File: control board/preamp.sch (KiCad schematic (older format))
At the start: 51 parts, among them U201 TL972, U202 MCP42100_VOL, U203 MCP42100_TREB, U204 MCP42100_BASS, U205 TL972

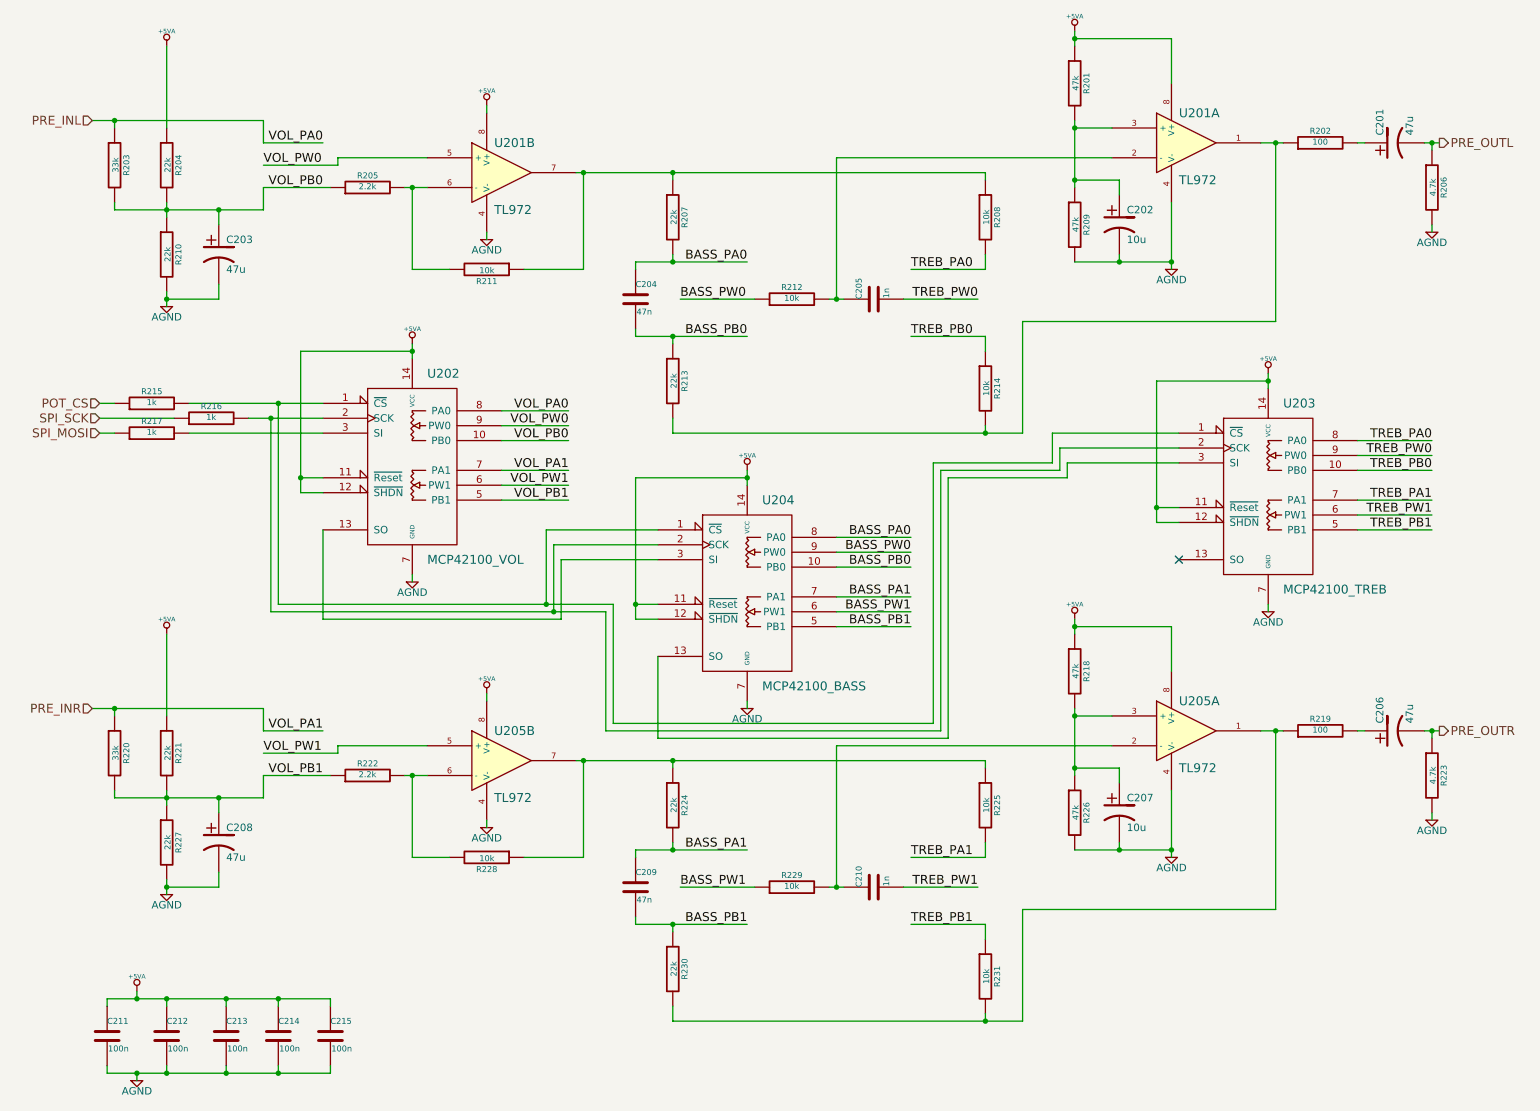
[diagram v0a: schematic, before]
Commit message: Fix capacitor polarity & prep for SMT
The control board and preamp are being prepared for SMT, and the CP1
module does not associate polarity correctly.
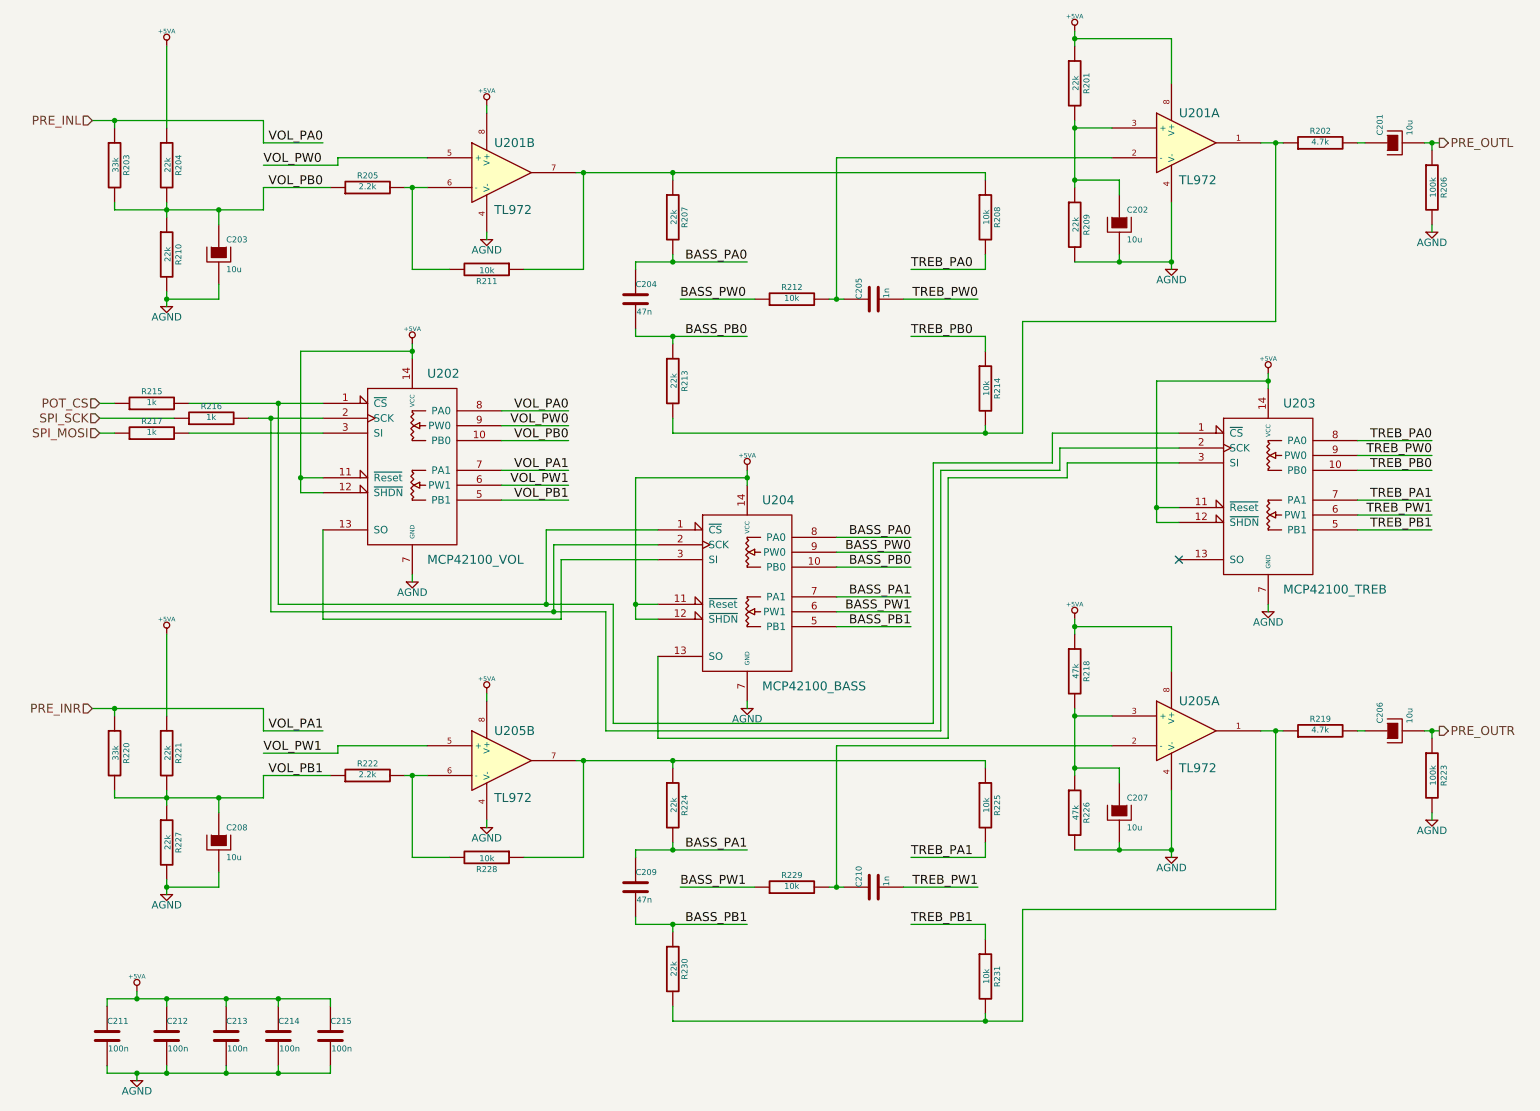
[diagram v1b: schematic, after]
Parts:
- removed C201, C203, C206, C208: 47u, ~, symbol CP1
- removed C202, C207: 10u, ~, symbol CP1
- added C201, C202, C203, C206, C207, C208: 10u, ~, symbol CAPAPOL
- R201, R209: value 47k -> 22k
- R202, R219: value 100 -> 4.7k
- R206, R223: value 4.7k -> 100k
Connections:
- net AGND: now also C202.2, C203.2, C207.2, C208.2
- net PRE_OUTL: now also C201.2
- net PRE_OUTR: now also C206.2
- net VOL_PB0: now also C203.1
- net VOL_PB1: now also C208.1
- net at R201.2, R209.1, U201.3 (+): now also C202.1
- net at R202.2: now also C201.1
- net at R218.2, R226.1, U205.3 (+): now also C207.1
- net at R219.2: now also C206.1
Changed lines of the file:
@@
 Sheet 2 2
 Title "AIA Rev. B Control Board Preamp"
-Date "8 mar 2014"
+Date "11 apr 2014"
 Rev "B01"
 Comp "Ali Kocaturk"
@@
 F 3 "~" H 1450 2100 30  0000 C CNN
 	1    1450 2100
-	1    0    0    -1
-$EndComp
-$Comp
-L CP1 C203
-U 1 1 531AED4E
-P 1800 2100
-F 0 "C203" H 1850 2200 50  0000 L CNN
-F 1 "47u" H 1850 2000 50  0000 L CNN
-F 2 "~" H 1800 2100 60  0000 C CNN
-F 3 "~" H 1800 2100 60  0000 C CNN
-	1    1800 2100
 	1    0    0    -1
 $EndComp
@@
 P 7550 950
 F 0 "R201" V 7630 950 40  0000 C CNN
-F 1 "47k" V 7557 951 40  0000 C CNN
+F 1 "22k" V 7557 951 40  0000 C CNN
 F 2 "~" V 7480 950 30  0000 C CNN
 F 3 "~" H 7550 950 30  0000 C CNN
@@
 P 7550 1900
 F 0 "R209" V 7630 1900 40  0000 C CNN
-F 1 "47k" V 7557 1901 40  0000 C CNN
+F 1 "22k" V 7557 1901 40  0000 C CNN
 F 2 "~" V 7480 1900 30  0000 C CNN
 F 3 "~" H 7550 1900 30  0000 C CNN
 	1    7550 1900
-	1    0    0    -1
-$EndComp
-$Comp
-L CP1 C202
-U 1 1 531A9735
-P 7850 1900
-F 0 "C202" H 7900 2000 50  0000 L CNN
-F 1 "10u" H 7900 1800 50  0000 L CNN
-F 2 "~" H 7850 1900 60  0000 C CNN
-F 3 "~" H 7850 1900 60  0000 C CNN
-	1    7850 1900
 	1    0    0    -1
 $EndComp
@@
 P 9200 1350
 F 0 "R202" V 9280 1350 40  0000 C CNN
-F 1 "100" V 9207 1351 40  0000 C CNN
+F 1 "4.7k" V 9207 1351 40  0000 C CNN
 F 2 "~" V 9130 1350 30  0000 C CNN
 F 3 "~" H 9200 1350 30  0000 C CNN
@@
 $EndComp
 $Comp
-L CP1 C201
-U 1 1 531A9D72
-P 9700 1350
-F 0 "C201" H 9750 1450 50  0000 L CNN
-F 1 "47u" H 9750 1250 50  0000 L CNN
-F 2 "~" H 9700 1350 60  0000 C CNN
-F 3 "~" H 9700 1350 60  0000 C CNN
-	1    9700 1350
-	0    -1   -1   0
-$EndComp
-$Comp
 L R R206
 U 1 1 531A9D81
 P 9950 1650
 F 0 "R206" V 10030 1650 40  0000 C CNN
-F 1 "4.7k" V 9957 1651 40  0000 C CNN
+F 1 "100k" V 9957 1651 40  0000 C CNN
 F 2 "~" V 9880 1650 30  0000 C CNN
 F 3 "~" H 9950 1650 30  0000 C CNN
@@
 F 3 "~" H 1450 6050 30  0000 C CNN
 	1    1450 6050
-	1    0    0    -1
-$EndComp
-$Comp
-L CP1 C208
-U 1 1 531AA135
-P 1800 6050
-F 0 "C208" H 1850 6150 50  0000 L CNN
-F 1 "47u" H 1850 5950 50  0000 L CNN
-F 2 "~" H 1800 6050 60  0000 C CNN
-F 3 "~" H 1800 6050 60  0000 C CNN
-	1    1800 6050
 	1    0    0    -1
 $EndComp
@@
 	1    0    0    -1
 $EndComp
-$Comp
-L CP1 C207
-U 1 1 531AA1DD
-P 7850 5850
-F 0 "C207" H 7900 5950 50  0000 L CNN
-F 1 "10u" H 7900 5750 50  0000 L CNN
-F 2 "~" H 7850 5850 60  0000 C CNN
-F 3 "~" H 7850 5850 60  0000 C CNN
-	1    7850 5850
-	1    0    0    -1
-$EndComp
 Connection ~ 7550 5200
 Wire Wire Line
@@
 P 9200 5300
 F 0 "R219" V 9280 5300 40  0000 C CNN
-F 1 "100" V 9207 5301 40  0000 C CNN
+F 1 "4.7k" V 9207 5301 40  0000 C CNN
 F 2 "~" V 9130 5300 30  0000 C CNN
 F 3 "~" H 9200 5300 30  0000 C CNN
@@
 $EndComp
 $Comp
-L CP1 C206
-U 1 1 531AA205
-P 9700 5300
-F 0 "C206" H 9750 5400 50  0000 L CNN
-F 1 "47u" H 9750 5200 50  0000 L CNN
-F 2 "~" H 9700 5300 60  0000 C CNN
-F 3 "~" H 9700 5300 60  0000 C CNN
-	1    9700 5300
-	0    -1   -1   0
-$EndComp
-$Comp
 L R R223
 U 1 1 531AA20B
 P 9950 5600
 F 0 "R223" V 10030 5600 40  0000 C CNN
-F 1 "4.7k" V 9957 5601 40  0000 C CNN
+F 1 "100k" V 9957 5601 40  0000 C CNN
 F 2 "~" V 9880 5600 30  0000 C CNN
 F 3 "~" H 9950 5600 30  0000 C CNN
@@
 	2550 7600 2550 7550
 Connection ~ 2200 7600
+$Comp
+L CAPAPOL C203
+U 1 1 53488C60
+P 1800 2100
+F 0 "C203" H 1850 2200 40  0000 L CNN
+F 1 "10u" H 1850 2000 40  0000 L CNN
+F 2 "~" H 1900 1950 30  0000 C CNN
+F 3 "~" H 1800 2100 300 0000 C CNN
+	1    1800 2100
+	1    0    0    -1
+$EndComp
+$Comp
+L CAPAPOL C202
+U 1 1 53488C7C
+P 7850 1900
+F 0 "C202" H 7900 2000 40  0000 L CNN
+F 1 "10u" H 7900 1800 40  0000 L CNN
+F 2 "~" H 7950 1750 30  0000 C CNN
+F 3 "~" H 7850 1900 300 0000 C CNN
+	1    7850 1900
+	1    0    0    -1
+$EndComp
+$Comp
+L CAPAPOL C201
+U 1 1 53488C8C
+P 9700 1350
+F 0 "C201" H 9750 1450 40  0000 L CNN
+F 1 "10u" H 9750 1250 40  0000 L CNN
+F 2 "~" H 9800 1200 30  0000 C CNN
+F 3 "~" H 9700 1350 300 0000 C CNN
+	1    9700 1350
+	0    -1   -1   0
+$EndComp
+$Comp
+L CAPAPOL C208
+U 1 1 53488C9C
+P 1800 6050
+F 0 "C208" H 1850 6150 40  0000 L CNN
+F 1 "10u" H 1850 5950 40  0000 L CNN
+F 2 "~" H 1900 5900 30  0000 C CNN
+F 3 "~" H 1800 6050 300 0000 C CNN
+	1    1800 6050
+	1    0    0    -1
+$EndComp
+$Comp
+L CAPAPOL C207
+U 1 1 53488CAC
+P 7850 5850
+F 0 "C207" H 7900 5950 40  0000 L CNN
+F 1 "10u" H 7900 5750 40  0000 L CNN
+F 2 "~" H 7950 5700 30  0000 C CNN
+F 3 "~" H 7850 5850 300 0000 C CNN
+	1    7850 5850
+	1    0    0    -1
+$EndComp
+$Comp
+L CAPAPOL C206
+U 1 1 53488CCB
+P 9700 5300
+F 0 "C206" H 9750 5400 40  0000 L CNN
+F 1 "10u" H 9750 5200 40  0000 L CNN
+F 2 "~" H 9800 5150 30  0000 C CNN
+F 3 "~" H 9700 5300 300 0000 C CNN
+	1    9700 5300
+	0    -1   -1   0
+$EndComp
 $EndSCHEMATC
